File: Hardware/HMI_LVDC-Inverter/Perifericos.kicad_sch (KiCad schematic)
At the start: 24 parts, among them J2 Conn_01x01_Pin, J3 Conn_01x01_Pin, J4 Conn_01x01_Pin, J5 Conn_01x01_Pin, J6 Conn_01x01_Pin, J7 Conn_01x01_Pin, J8 Conn_01x04_Pin, SW1 SW_MEC_5E, SW2 SW_MEC_5E, SW3 SW_MEC_5E, SW4 SW_MEC_5E, SW5 SW_MEC_5E, SW6 SW_MEC_5E, SW7 SW_MEC_5E, SW8 SW_MEC_5E, SW9 SW_MEC_5E

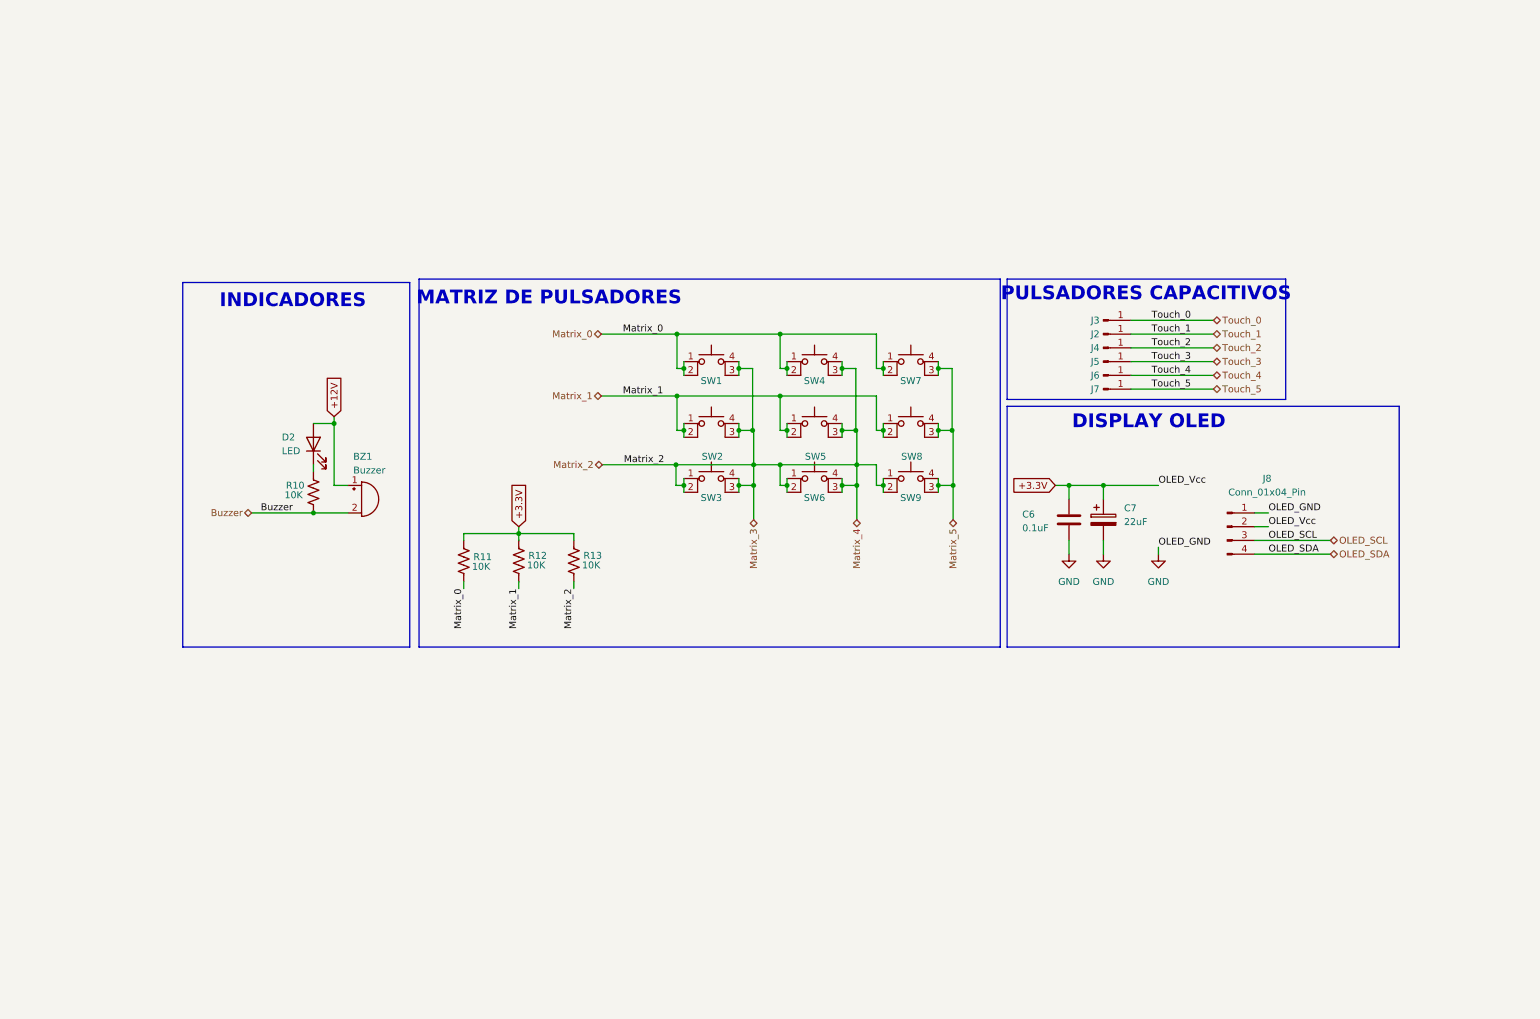
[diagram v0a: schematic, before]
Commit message: Cambios en los periféricos previo al viaje para poder seguir trabajándolo
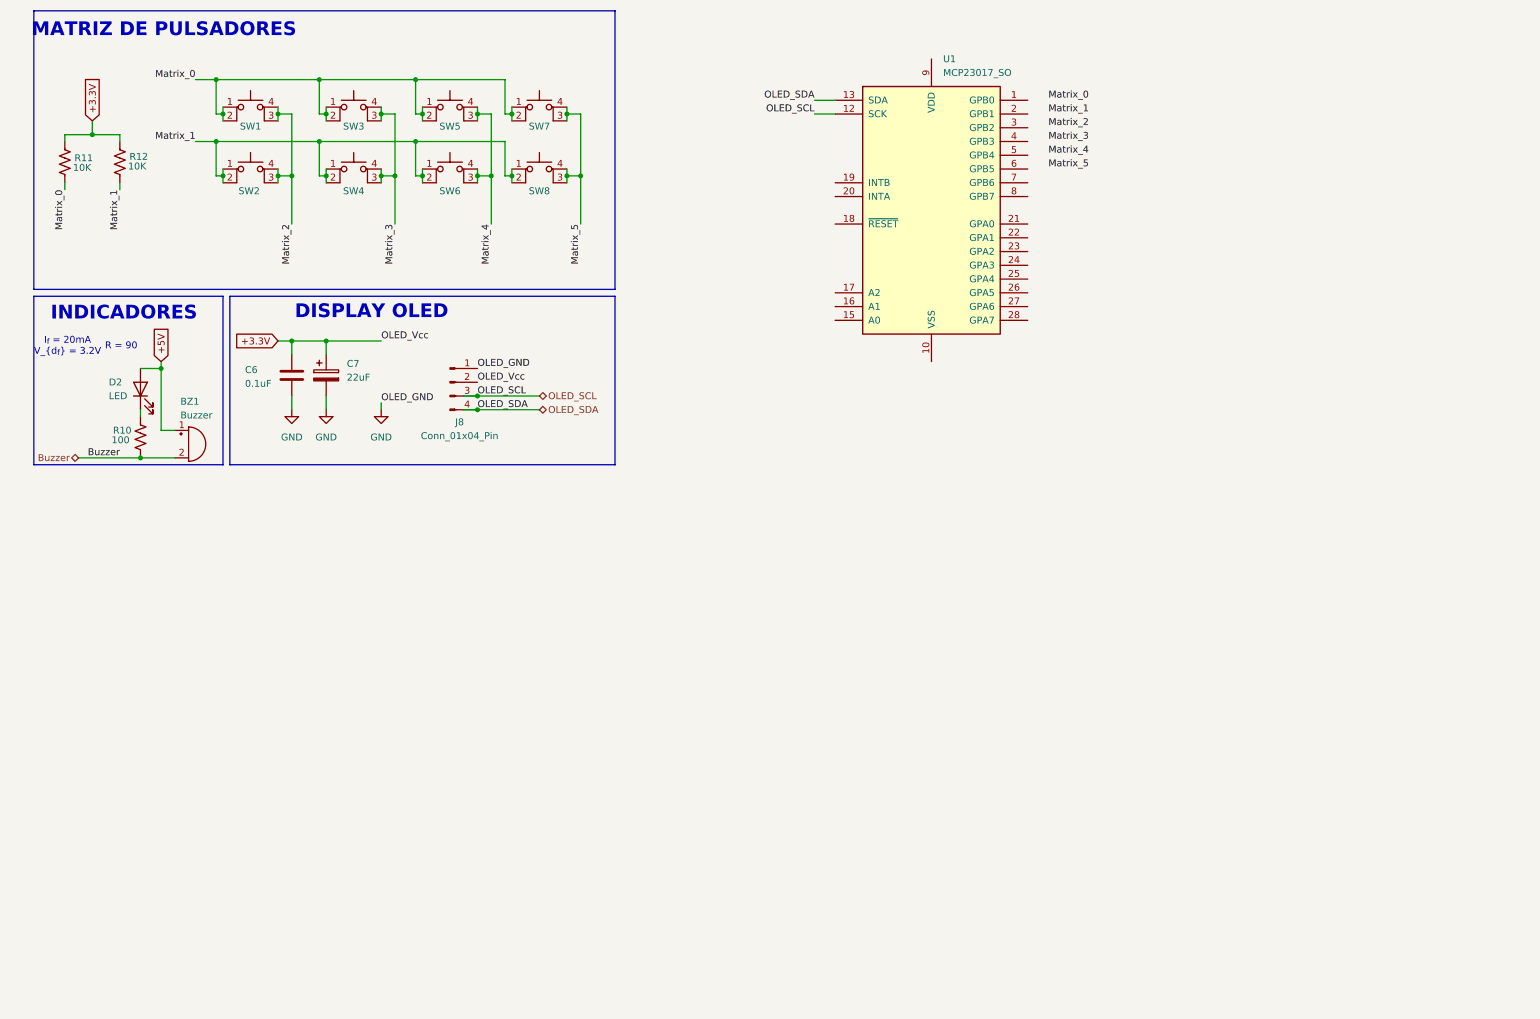
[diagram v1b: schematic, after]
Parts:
- removed J2, J3, J4, J5, J6, J7: Conn_01x01_Pin, symbol Connector:Conn_01x01_Pin
- removed R13: 10K, symbol Device:R_US
- removed SW3, SW6, SW9: SW_MEC_5E, Button_Switch_SMD:SW_MEC_5GSH9, symbol Switch:SW_MEC_5E
- added SW7, SW8: SW_MEC_5E, Button_Switch_SMD:SW_MEC_5GSH9, symbol Switch:SW_MEC_5E
- added U1: MCP23017_SO, Package_SO:SOIC-28W_7.5x17.9mm_P1.27mm, symbol Interface_Expansion:MCP23017_SO
- R10: value 10K -> 100
- renumbered SW4 to SW3, SW5 to SW4, SW7 to SW5, SW8 to SW6
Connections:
- net Matrix_0: now also SW7.1, SW7.2
- net Matrix_1: now also SW8.1, SW8.2
- net Matrix_2: no longer SW3.3 (K), SW3.4 (A), SW4.3 (K), SW4.4 (A)
- net Matrix_5: now also SW7.3 (K), SW7.4 (A), SW8.3 (K), SW8.4 (A); no longer SW5.3 (K), SW5.4 (A), SW6.3 (K), SW6.4 (A)
- net OLED_SCL: now also U1.12 (SCK)
- net OLED_SDA: now also U1.13 (SDA)
- net +12V renamed +5V
- new net Matrix_3: SW3.3 (K), SW3.4 (A), SW4.3 (K), SW4.4 (A)
- new net Matrix_4: SW5.3 (K), SW5.4 (A), SW6.3 (K), SW6.4 (A)
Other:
- note added: "I_{f} = 20mA V_{d_{f}} = 3.2V"
- note added: "R = 90"
- note removed: "PULSADORES CAPACITIVOS"
- moved on the sheet: BZ1, C6, C7, D2, J8, R10, R11, R12, SW1, SW2, SW3, SW4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

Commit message: Termino de hacer las simulaciones de los periféricos. Completo los valores de componentes en esquemáticos
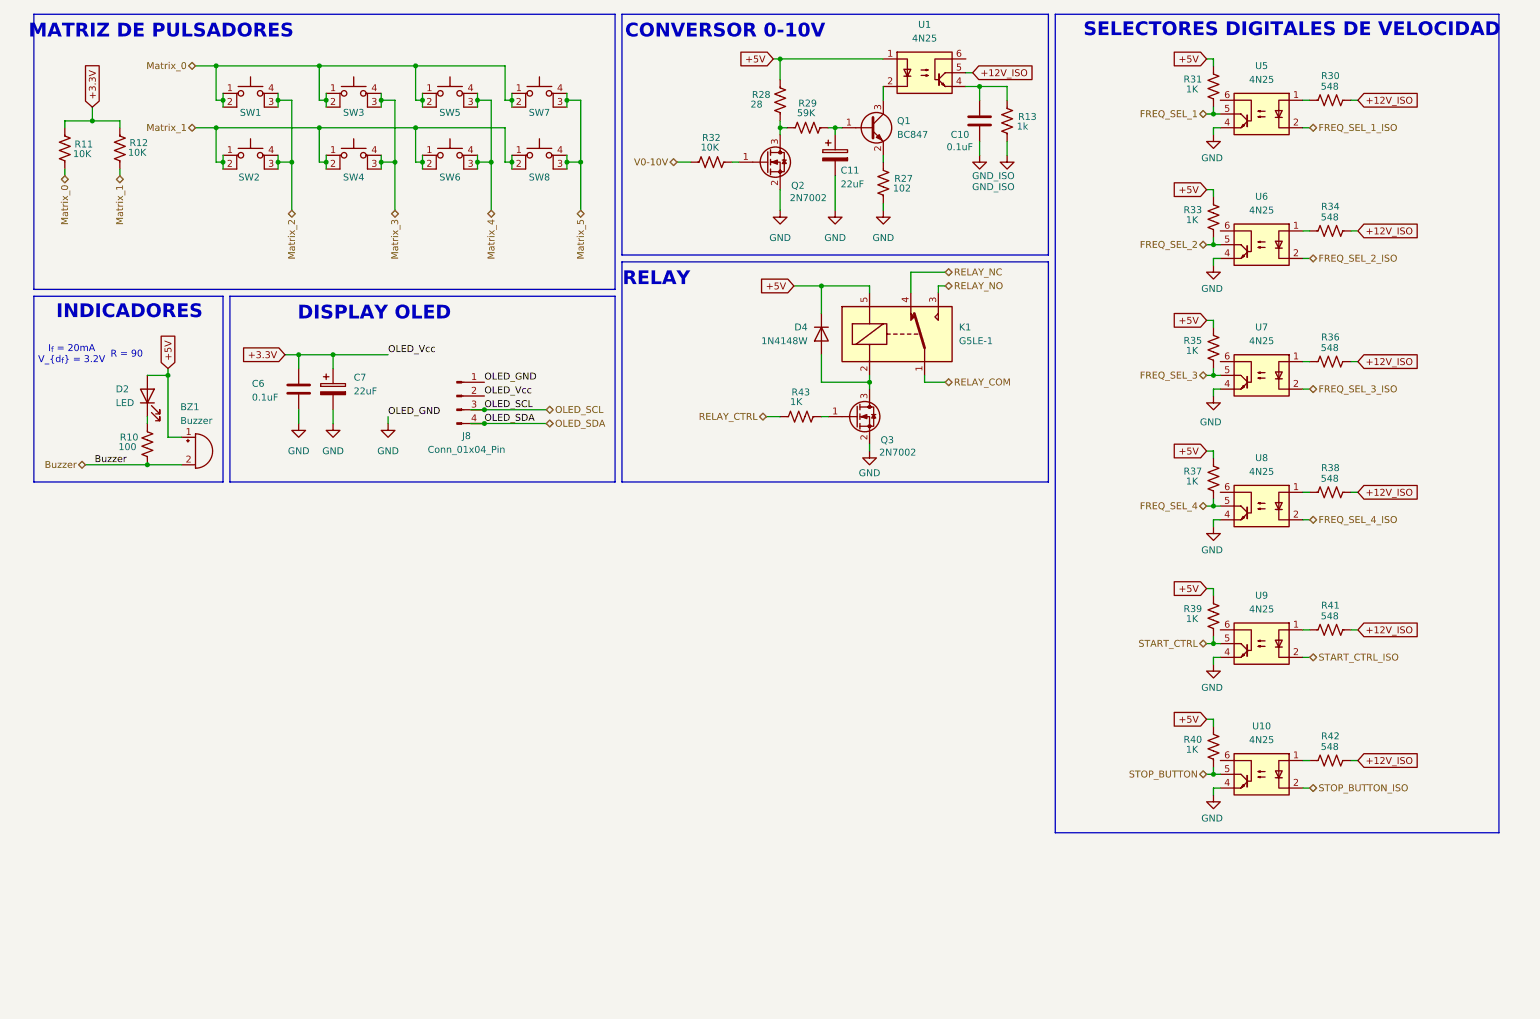
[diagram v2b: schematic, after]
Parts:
- removed U1: MCP23017_SO, Package_SO:SOIC-28W_7.5x17.9mm_P1.27mm, symbol Interface_Expansion:MCP23017_SO
- added C10: 0.1uF, Capacitor_SMD:C_0603_1608Metric, symbol Device:C
- added C11: 22uF, Capacitor_SMD:C_1206_3216Metric, symbol Device:C_Polarized
- added D4: 1N4148W, Diode_SMD:D_SOD-123, symbol Diode:1N4148W
- added K1: G5LE-1, Relay_THT:Relay_SPDT_Omron_G2RL-1, symbol Relay:G5LE-1
- added Q1: BC847, Package_TO_SOT_THT:TO-39-3, symbol Transistor_BJT:BC847
- added Q2, Q3: 2N7002, Package_TO_SOT_SMD:SOT-23, symbol Transistor_FET:2N7002
- added R13: 1k, symbol Device:R_US
- added R27: 102, symbol Device:R_US
- added R28: 28, symbol Device:R_US
- added R29: 59K, symbol Device:R_US
- added R30, R34, R36, R38, R41, R42: 548, symbol Device:R_US
- added R31, R33, R35, R37, R39, R40, R43: 1K, symbol Device:R_US
- added R32: 10K, symbol Device:R_US
- added U1, U10, U5, U6, U7, U8, U9: 4N25, Package_DIP:DIP-6_W7.62mm_SMDSocket_SmallPads, symbol Isolator:4N25
- C7: footprint Inductor_SMD:L_1206_3216Metric -> Capacitor_SMD:C_1206_3216Metric
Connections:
- net +5V: now also D4.1 (K), K1.5, R28.2, R31.2, R33.2, R35.2, R37.2, R39.2, R40.2, U1.1
- net GND: now also C11.2, Q2.2 (S), Q3.2 (S), R27.1, U10.4, U5.4, U6.4, U7.4, U8.4, U9.4
- new net: D4.2 (A), K1.2, Q3.3 (D)
- new net: C10.1, R13.2, U1.4
- new net: R36.1, U7.1
- new net: Q3.1 (G), R43.2
- new net: R38.1, U8.1
- new net: Q2.3 (D), R28.1, R29.1
- new net: C11.1, Q1.1 (B), R29.2
- new net: R41.1, U9.1
- new net: Q1.3 (C), U1.2
- new net: Q1.2 (E), R27.2
- new net: R42.1, U10.1
- new net: R34.1, U6.1
- new net: R30.1, U5.1
- new net: Q2.1 (G), R32.2
- new net +12V_ISO: R30.2, R34.2, R36.2, R38.2, R41.2, R42.2, U1.5
- new net FREQ_SEL_1: R31.1, U5.5
- new net FREQ_SEL_1_ISO: U5.2
- new net FREQ_SEL_2: R33.1, U6.5
- new net FREQ_SEL_2_ISO: U6.2
- new net FREQ_SEL_3: R35.1, U7.5
- new net FREQ_SEL_3_ISO: U7.2
- new net FREQ_SEL_4: R37.1, U8.5
- new net FREQ_SEL_4_ISO: U8.2
- new net GND_ISO: C10.2, R13.1
- new net RELAY_COM: K1.1
- new net RELAY_CTRL: R43.1
- new net RELAY_NC: K1.4
- new net RELAY_NO: K1.3
- new net START_CTRL: R39.1, U9.5
- new net START_CTRL_ISO: U9.2
- new net STOP_BUTTON: R40.1, U10.5
- new net STOP_BUTTON_ISO: U10.2
- new net V0-10V: R32.1
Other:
- note added: "CONVERSOR 0-10V"
- note added: "RELAY"
- note added: "SELECTORES DIGITALES DE VELOCIDAD"
- moved on the sheet: BZ1, C6, C7, D2, J8, R10, R11, R12, SW1, SW2, SW3, SW4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

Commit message: Terminado el esquemático del HMI
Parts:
- J8: footprint Connector_DIN:DIN41612_B3_2x5_Female_Vertical_THT -> Connector_PinHeader_1.00mm:PinHeader_1x04_P1.00mm_Vertical
- R10: value 100 -> 102
- R13: value 1k -> 1K
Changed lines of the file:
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@@
 	)
 	(junction
-		(at 96.52 88.9)
-		(diameter 0)
-		(color 0 0 0 0)
-	)
-	(junction
 		(at 46.99 22.86)
 		(diameter 0)
@@
 	)
 	(junction
-		(at 96.52 86.36)
-		(diameter 0)
-		(color 0 0 0 0)
-	)
-	(junction
 		(at 60.96 40.64)
 		(diameter 0)
@@
 	(wire
 		(pts
-			(xy 93.98 86.36) (xy 96.52 86.36)
-		)
-		(stroke
-			(width 0)
-			(type default)
-		)
-	)
-	(wire
-		(pts
 			(xy 83.82 22.86) (xy 83.82 29.21)
 		)
@@
 	(wire
 		(pts
-			(xy 93.98 88.9) (xy 96.52 88.9)
-		)
-		(stroke
-			(width 0)
-			(type default)
-		)
-	)
-	(wire
-		(pts
 			(xy 256.54 127) (xy 257.81 127)
 		)
@@
 			)
 		)
-		(property "Value" "1k"
+		(property "Value" "1K"
 			(at 194.818 34.036 0)
 			(effects
@@
 			)
 		)
-		(property "Footprint" "Connector_DIN:DIN41612_B3_2x5_Female_Vertical_THT"
+		(property "Footprint" "Connector_PinHeader_1.00mm:PinHeader_1x04_P1.00mm_Vertical"
 			(at 91.44 83.82 0)
 			(effects
@@
 			)
 		)
-		(property "Value" "100"
+		(property "Value" "102"
 			(at 28.956 93.218 0)
 			(effects

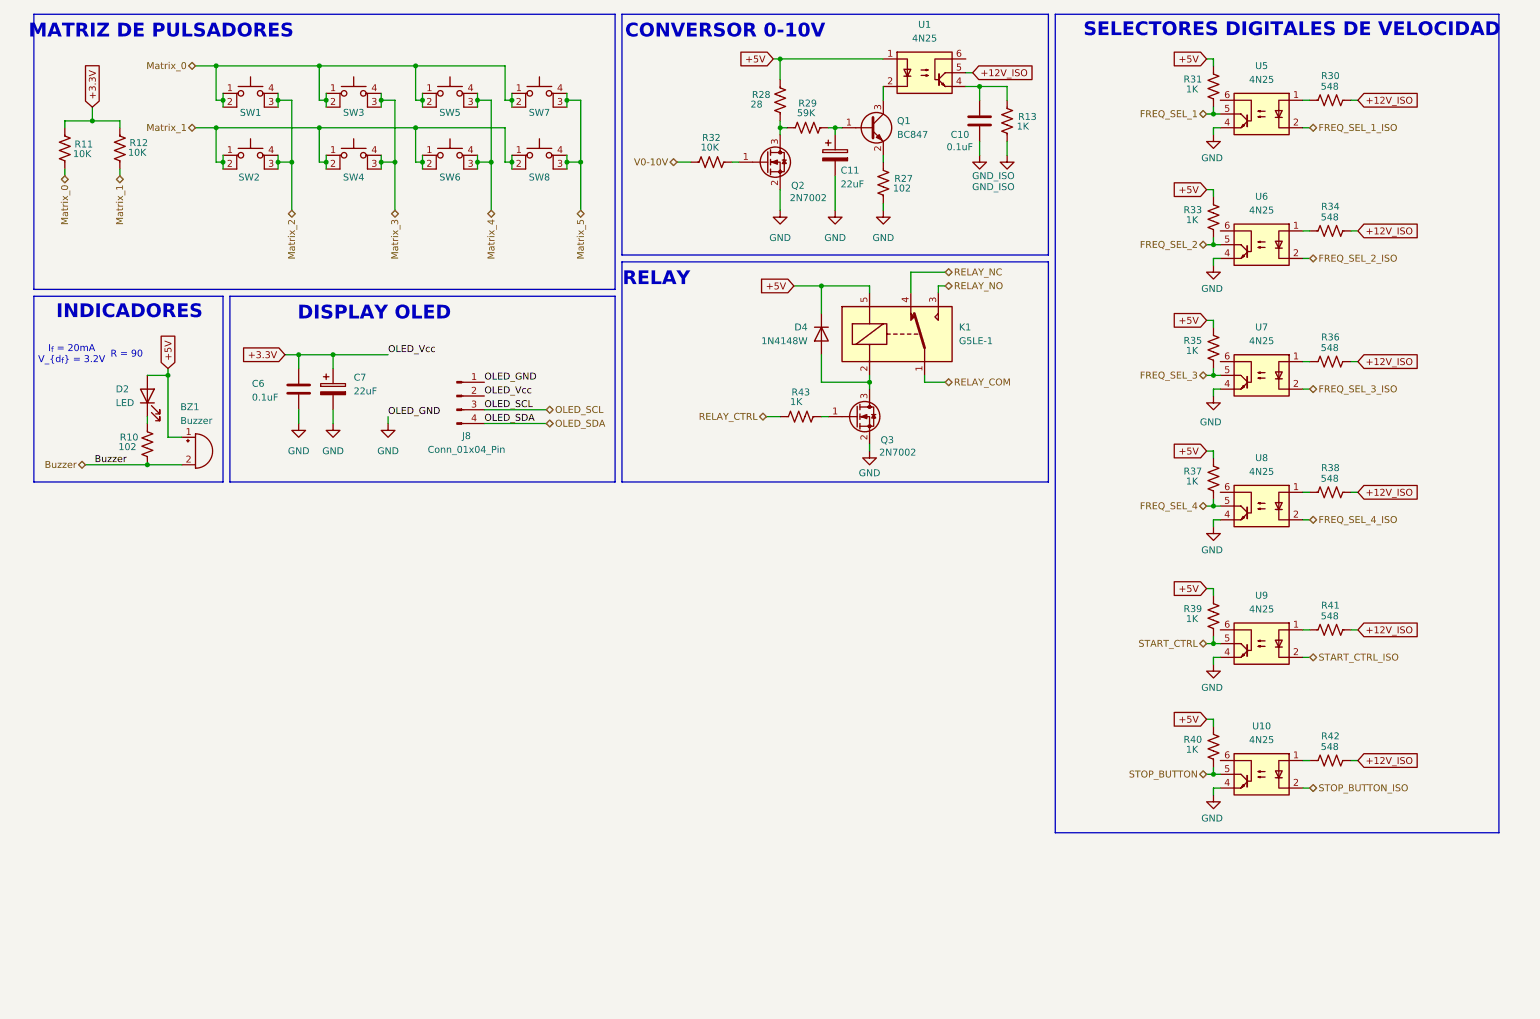
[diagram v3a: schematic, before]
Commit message: Avance con el esquemático, faltan definir algunas etiquetas que no las encontré
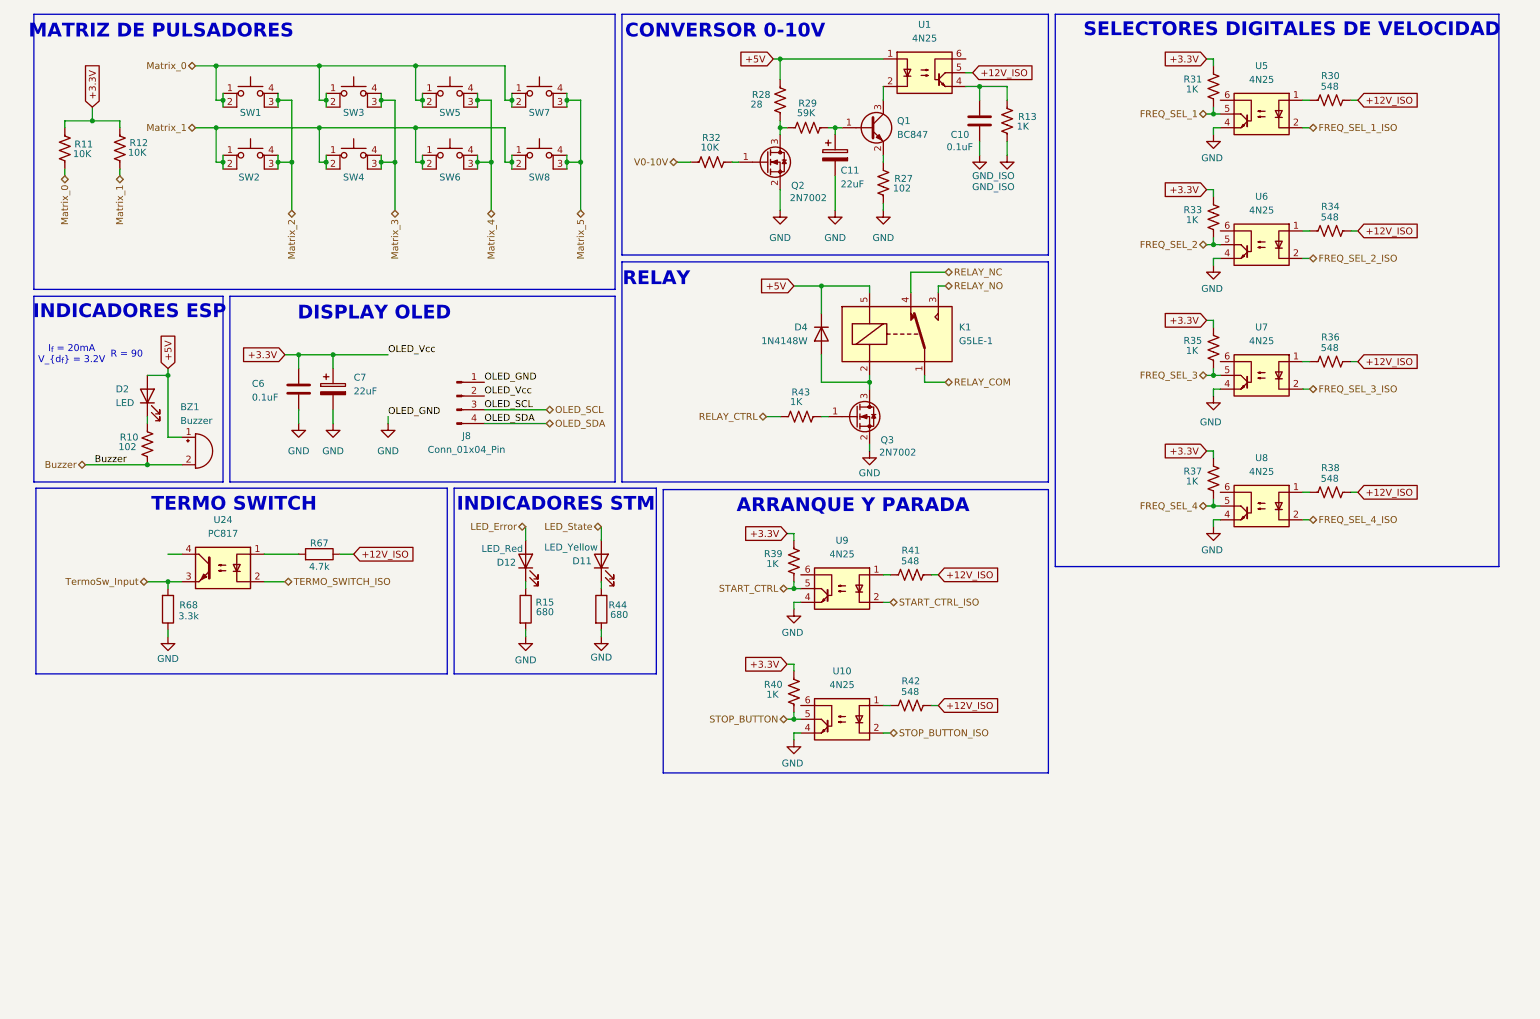
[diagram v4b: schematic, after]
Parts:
- added D11: LED_Yellow, LED_SMD:LED_0603_1608Metric_Pad1.05x0.95mm_HandSolder, symbol Device:LED
- added D12: LED_Red, LED_SMD:LED_0603_1608Metric_Pad1.05x0.95mm_HandSolder, symbol Device:LED
- added R15, R44: 680, Resistor_SMD:R_0603_1608Metric_Pad0.98x0.95mm_HandSolder, symbol Device:R
- added R67: 4.7k, Resistor_SMD:R_0603_1608Metric_Pad0.98x0.95mm_HandSolder, symbol Device:R
- added R68: 3.3k, Resistor_SMD:R_0603_1608Metric_Pad0.98x0.95mm_HandSolder, symbol Device:R
- added U24: PC817, Package_DIP:DIP-4_W7.62mm_SMDSocket_SmallPads, symbol Isolator:PC817
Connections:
- net +12V_ISO: now also R67.1
- net +3.3V: now also R31.2, R33.2, R35.2, R37.2, R39.2, R40.2
- net +5V: no longer R31.2, R33.2, R35.2, R37.2, R39.2, R40.2
- net GND: now also R15.2, R44.2, R68.1
- new net: D12.1 (K), R15.1
- new net: R67.2, U24.1
- new net: D11.1 (K), R44.1
- new net LED_Error: D12.2 (A)
- new net LED_State: D11.2 (A)
- new net TERMO_SWITCH_ISO: U24.2
- new net TermoSw_Input: R68.2, U24.3
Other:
- note added: "ARRANQUE Y PARADA"
- note added: "INDICADORES ESP"
- note added: "INDICADORES STM"
- note added: "TERMO SWITCH"
- note removed: "INDICADORES"
- moved on the sheet: R39, R40, R41, R42, U10, U9
